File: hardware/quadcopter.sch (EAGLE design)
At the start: 62 parts, among them J1 AVR_SPI_PRG_6NS, J2 HEADER-4POS-2X2-0.1IN-FEMALE-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, J3 HEADER-10POSTH-254X10, J4 HEADER-4POS-0.1IN-FEMALE-SMD-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, Q1 MOSFET-SI2302CDS-T1-E3CT-ND, Q2 MOSFET-SI2302CDS-T1-E3CT-ND, Q3 MOSFET-SI2302CDS-T1-E3CT-ND, Q4 MOSFET-SI2302CDS-T1-E3CT-ND, Q5 MOSFET-SI2302CDS-T1-E3CT-ND, Q6 MOSFET-SI2302CDS-T1-E3CT-ND, SW1 PUSHBUTTON_SMD-VERTICAL-1, U1 ATMEGA128RFA1, U2 LSM-IMU-497-18367-1-NDIMU, Y1 CRYSTAL5X3

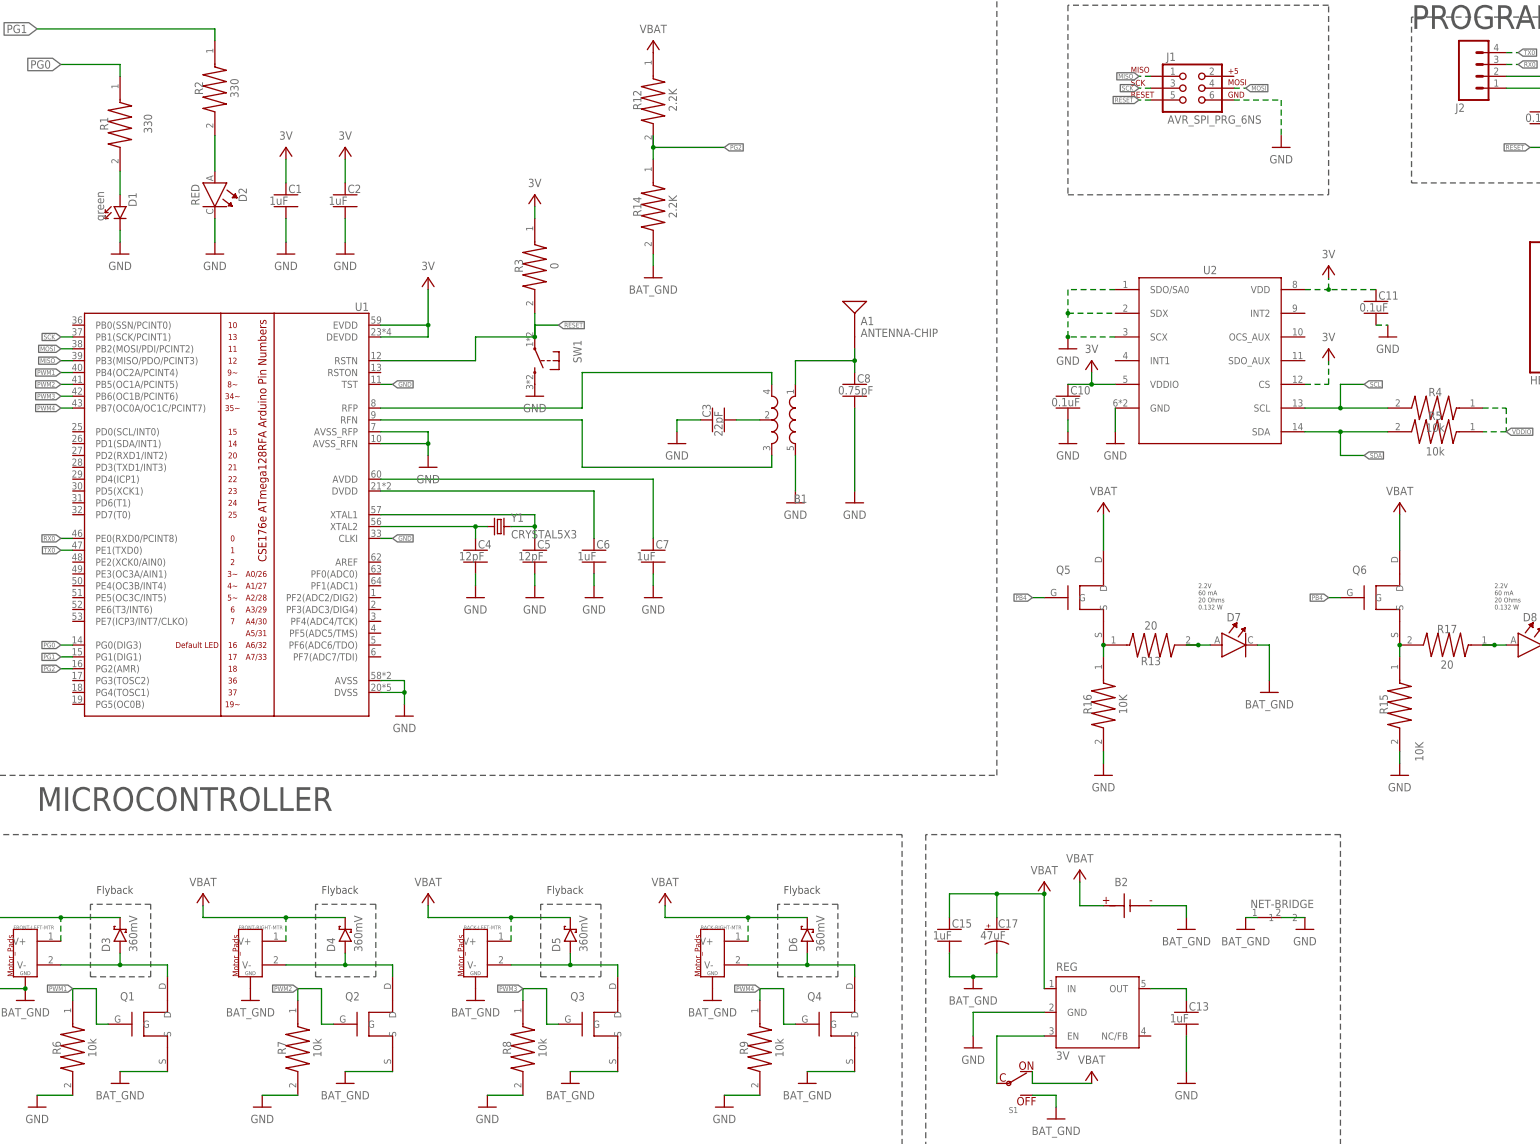
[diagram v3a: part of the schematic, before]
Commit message: 2 new resistors
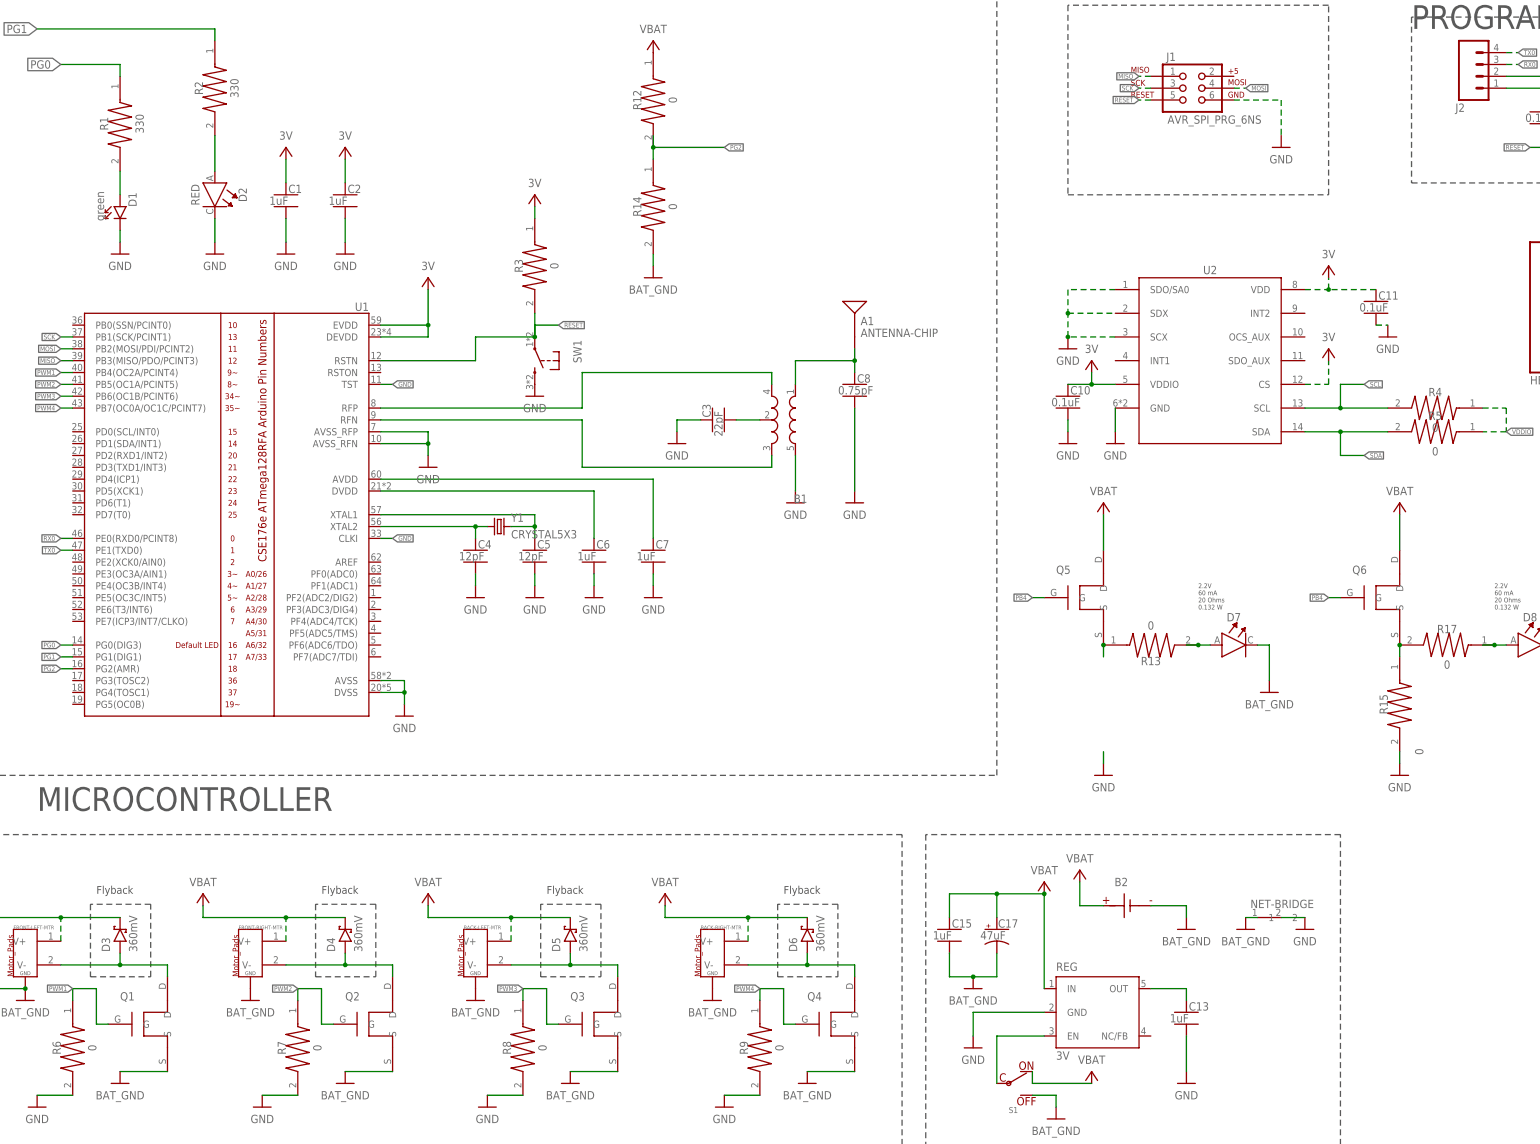
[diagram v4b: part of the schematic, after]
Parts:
- removed R16: 10K, custom.lbr:MY-RESISTOR-08050OHMRES
- R1, R2: device custom:MY-RESISTOR-08050OHMRES -> custom.lbr:MY-RESISTOR-0805330OHMRES
- R12, R14: value 2.2K -> 0
- R13, R17: value 20 -> 0
- R15: value 10K -> 0
- R4, R5, R6, R7, R8, R9: value 10k -> 0
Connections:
- net GND: no longer R16.2
- net N$19: no longer R16.1

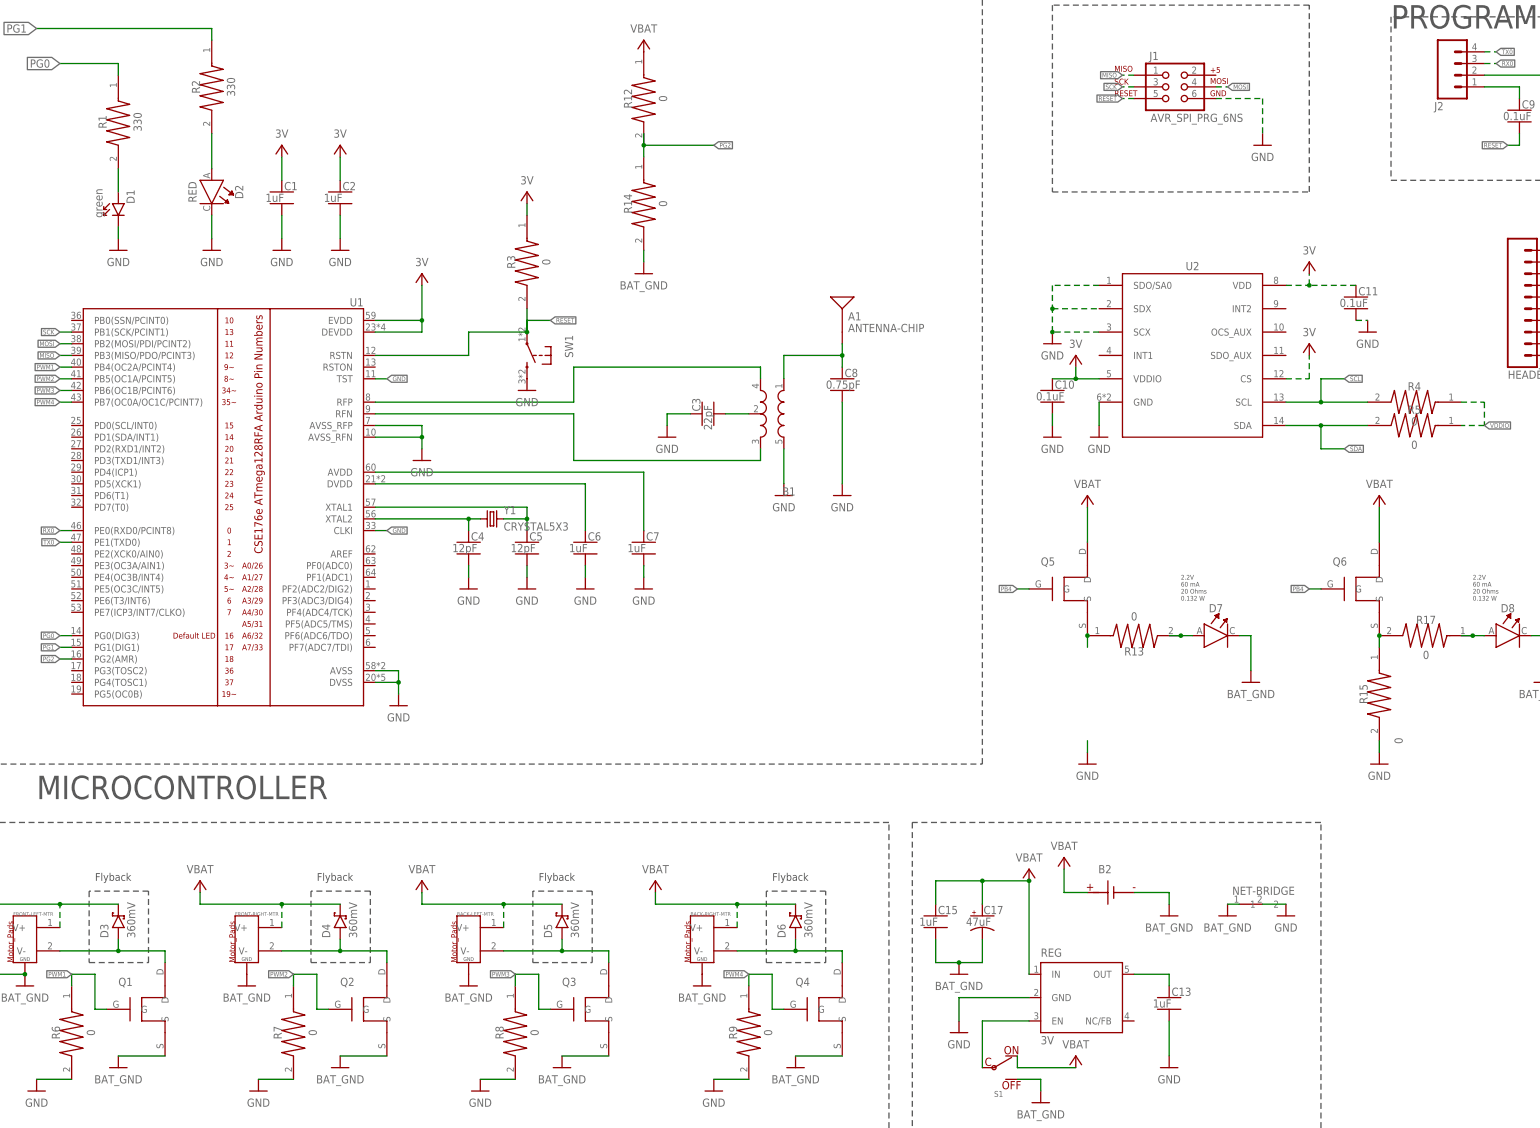
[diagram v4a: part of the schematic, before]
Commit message: resistors fixed with variants
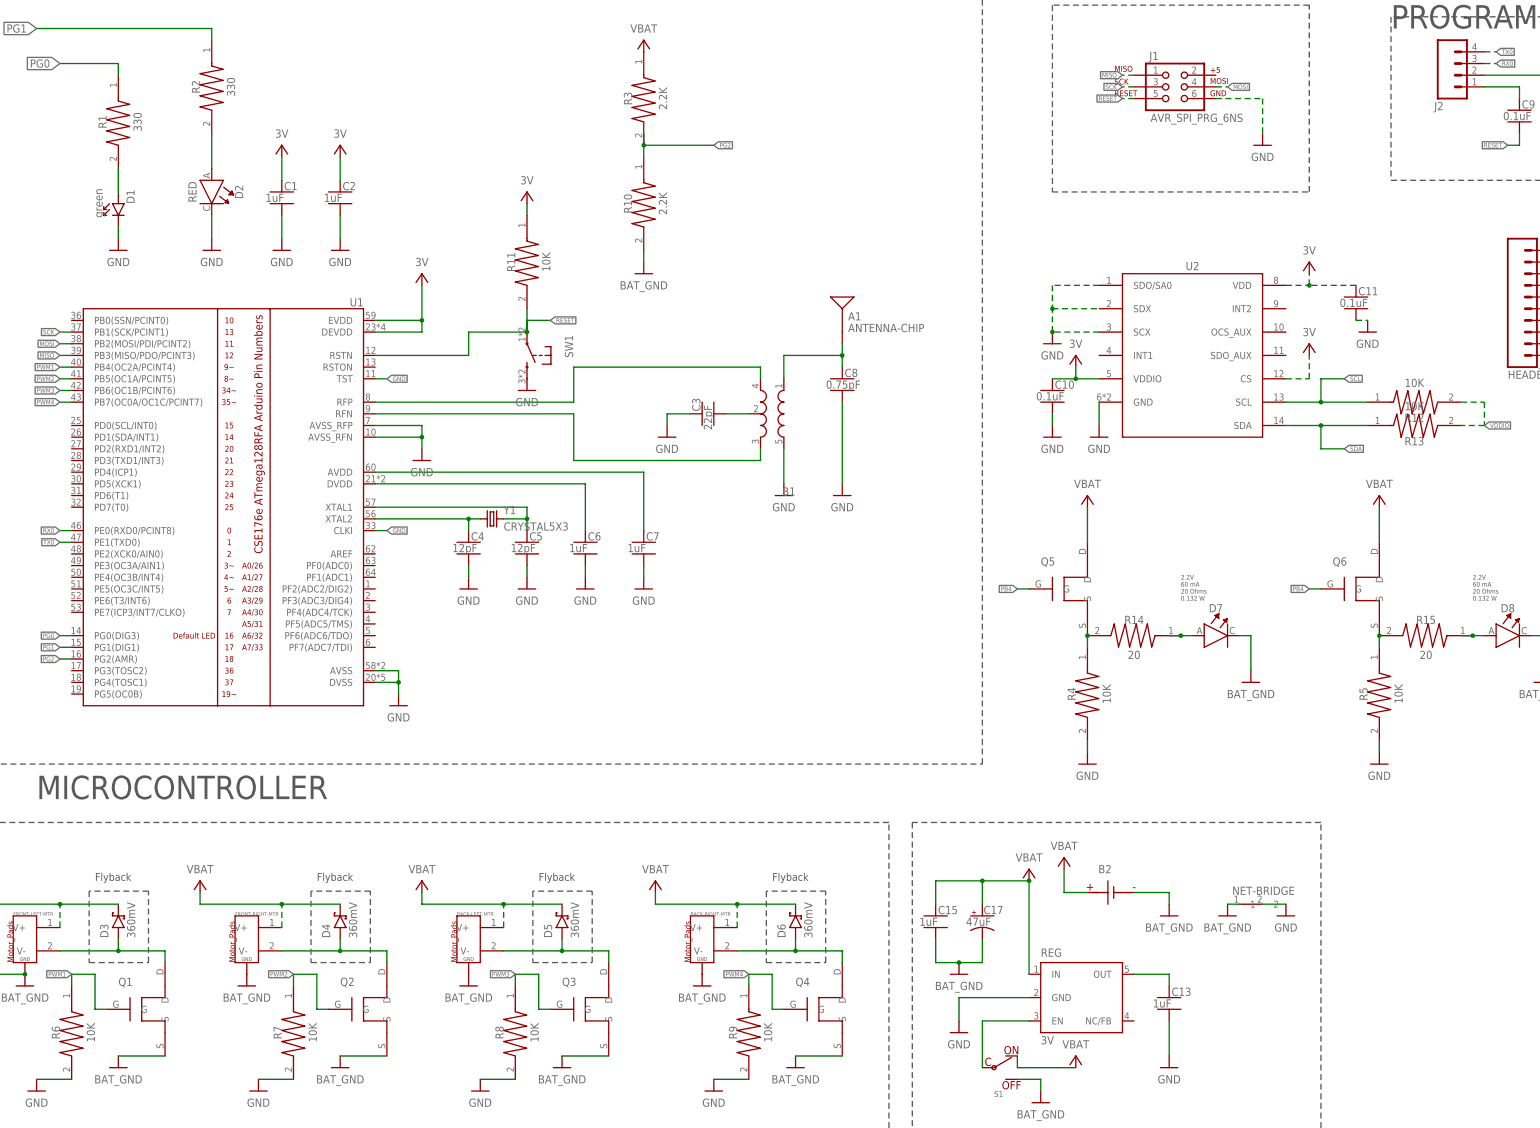
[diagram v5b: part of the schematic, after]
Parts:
- removed R17: 0, custom.lbr:MY-RESISTOR-08050OHMRES
- added R10: 2.2K, custom.lbr:MY-RESISTOR-08052.2KOHMRES
- added R11: 10K, custom.lbr:MY-RESISTOR-080510KOHMRES
- R12, R13, R4, R5, R6, R7, R8, R9: value 0 -> 10K; device custom.lbr:MY-RESISTOR-08050OHMRES -> custom.lbr:MY-RESISTOR-080510KOHMRES
- R14, R15: value 0 -> 20; device custom.lbr:MY-RESISTOR-08050OHMRES -> custom.lbr:MY-RESISTOR-080520OHMRES
- R3: value 0 -> 2.2K; device custom.lbr:MY-RESISTOR-08050OHMRES -> custom.lbr:MY-RESISTOR-08052.2KOHMRES
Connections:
- net 3V: now also R11.1; no longer R3.1
- net BAT_GND: now also R10.2; no longer R14.2
- net GND: now also R4.2, R5.2; no longer R15.2
- net N$12: now also R14.1; no longer R13.2
- net N$13: now also R15.2, R5.1; no longer R15.1, R17.2
- net N$19: now also R14.2, R4.1; no longer R13.1
- net N$21: now also R15.1; no longer R17.1
- net PG2: now also R10.1, R3.2; no longer R12.2, R14.1
- net RESET: now also R11.2; no longer R3.2
- net SCL: now also R12.1; no longer R4.2
- net SDA: now also R13.1; no longer R5.2
- net VBAT: now also R3.1; no longer R12.1
- net VDDIO: now also R12.2, R13.2; no longer R4.1, R5.1
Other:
- moved on the sheet: R12, R13, R14, R15, R3, R4, R5
